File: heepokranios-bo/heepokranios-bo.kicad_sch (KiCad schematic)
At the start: 146 parts, among them J1 Conn_02x02_Odd_Even, J11 PGA_13x13, J14 Conn_02x03_Odd_Even, J15 Conn_02x08_Odd_Even, J16 Conn_02x03_Odd_Even, J17 Conn_02x03_Odd_Even, J2 Conn_02x02_Odd_Even, J21 Conn_01x02, J26 Conn_01x02, J27 Conn_01x02, J29 Conn_01x02, J3 Conn_02x03_Odd_Even, J30 Conn_01x02, J31 Conn_01x02, J32 Conn_01x02, J33 Conn_01x02, J34 Conn_01x02, J35 Conn_01x02, J36 Conn_01x02, J37 Conn_01x02, J38 Conn_01x02, J39 Conn_01x02, J4 Conn_02x03_Odd_Even, J40 Conn_01x02, J41 Conn_01x02, J42 Conn_01x02, J43 Conn_01x02, J48 Conn_01x02, J49 Conn_01x02, J5 Conn_02x03_Odd_Even, J6 Conn_02x04_Odd_Even, J8 Conn_02x03_Odd_Even, J9 Conn_02x02_Odd_Even, SW1 SW_Push, U1 BIWIN_DTS04GE_SMD

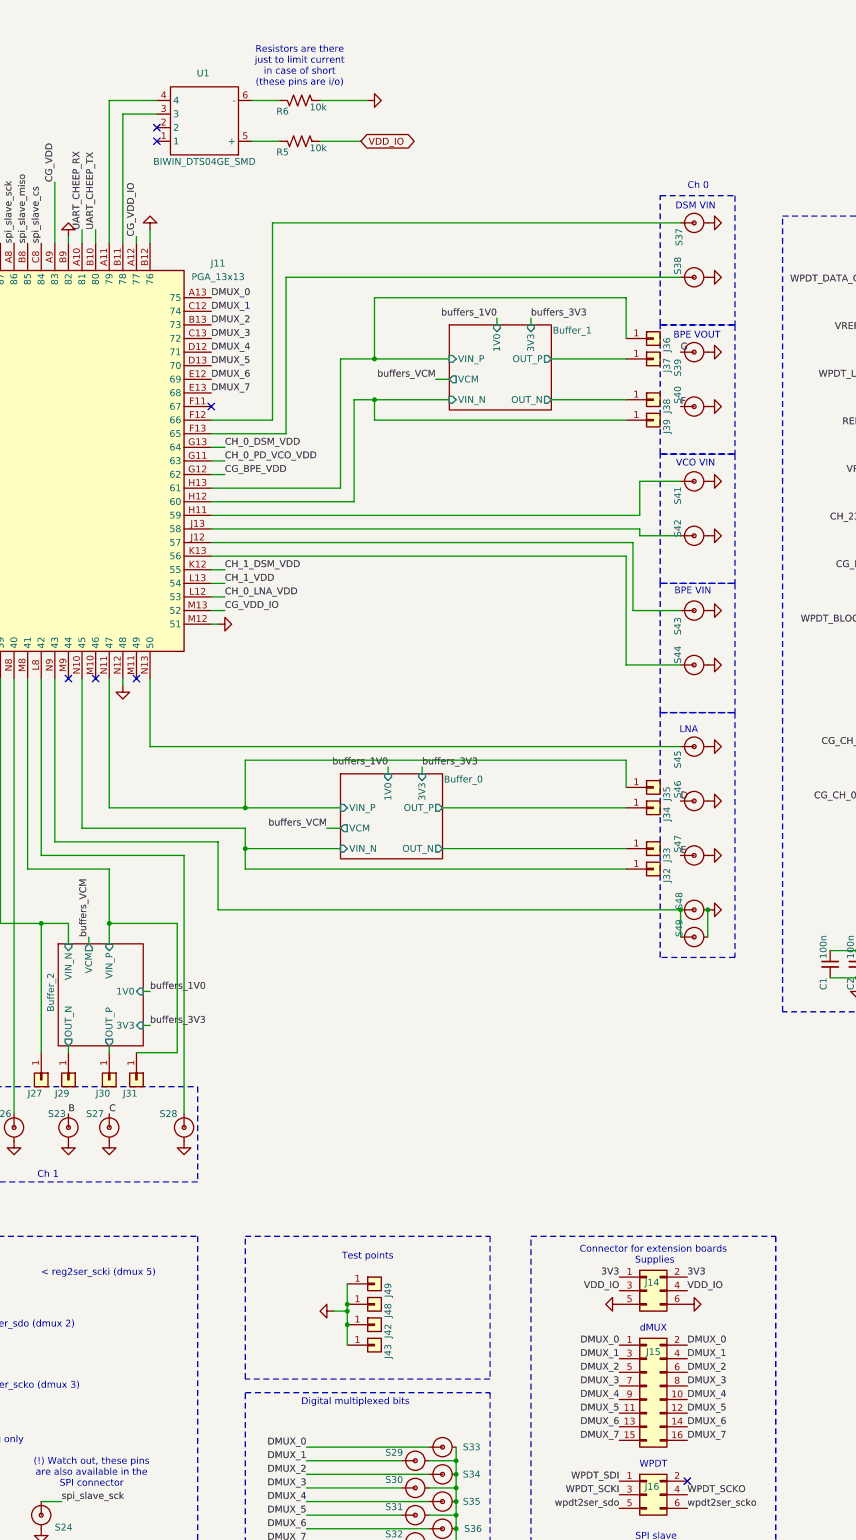
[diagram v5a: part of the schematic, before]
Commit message: Updated connector on bo
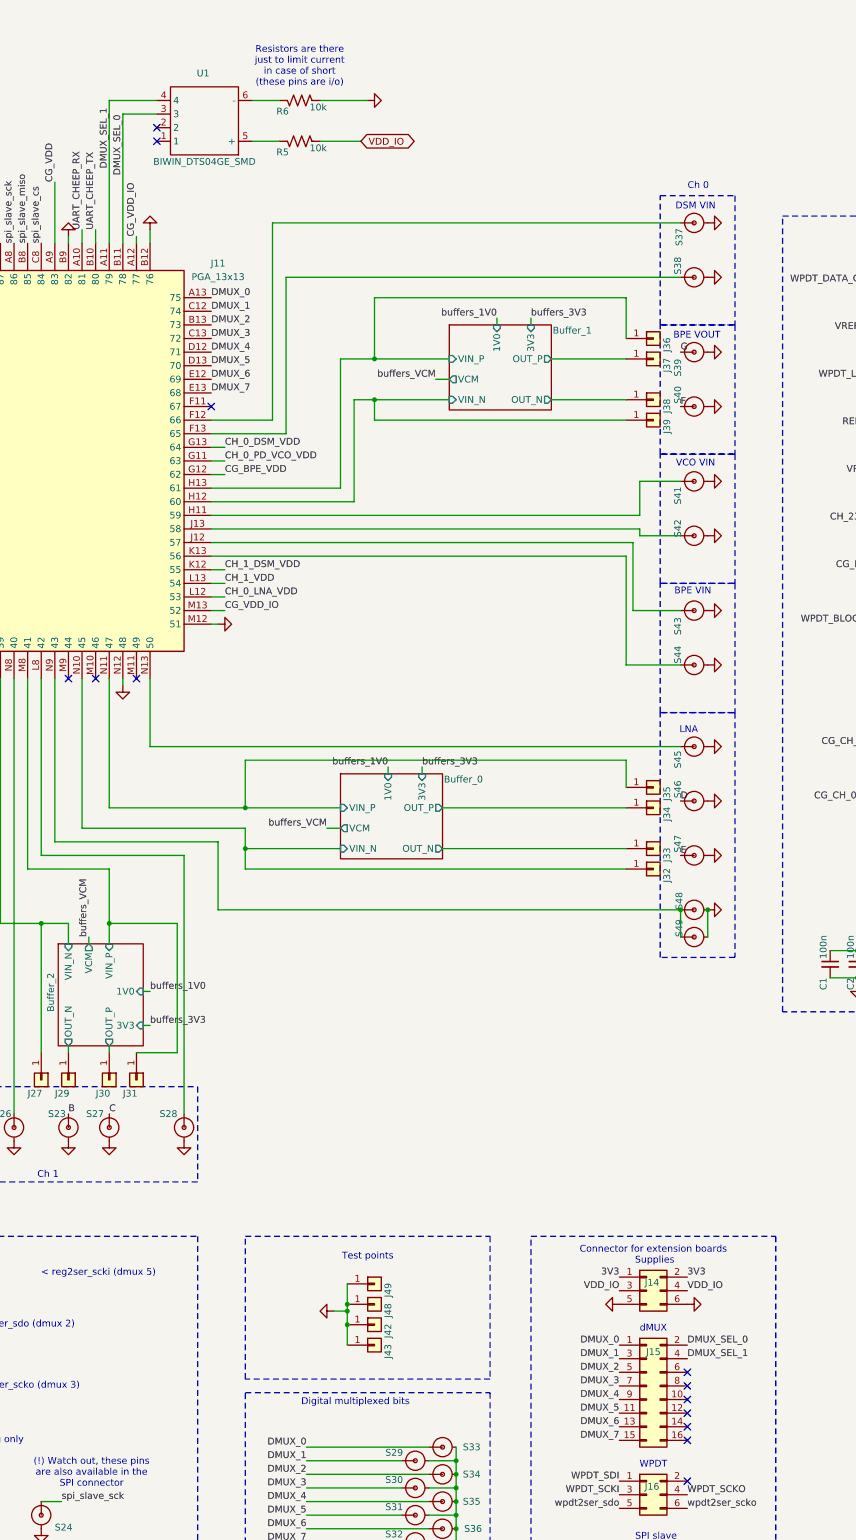
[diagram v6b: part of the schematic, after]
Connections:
- net DMUX_0: no longer J15.2 (Pin_2)
- net DMUX_1: no longer J15.4 (Pin_4)
- net DMUX_2: no longer J15.6 (Pin_6)
- net DMUX_3: no longer J15.8 (Pin_8)
- net DMUX_4: no longer J15.10 (Pin_10)
- net DMUX_5: no longer J15.12 (Pin_12)
- net DMUX_6: no longer J15.14 (Pin_14)
- net DMUX_7: no longer J15.16 (Pin_16)
- net DMUX_SEL_1: now reaches J11.A11 (79), U1.4
- net DMUX_SEL_1: now also J15.4 (Pin_4)
- net DMUX_SEL_0: now reaches J11.B11 (78), U1.3
- net DMUX_SEL_0: now also J15.2 (Pin_2)
- no-connect marks 112 -> 118
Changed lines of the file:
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@@
 	)
 	(no_connect
+		(at 394.97 364.49)
+	)
+	(no_connect
 		(at 209.55 86.36)
 	)
@@
 	)
 	(no_connect
+		(at 394.97 369.57)
+	)
+	(no_connect
 		(at 306.07 86.36)
 	)
@@
 	)
 	(no_connect
+		(at 394.97 367.03)
+	)
+	(no_connect
 		(at 224.79 86.36)
 	)
@@
 	)
 	(no_connect
+		(at 394.97 359.41)
+	)
+	(no_connect
 		(at 326.39 58.42)
 	)
@@
 	)
 	(no_connect
+		(at 394.97 361.95)
+	)
+	(no_connect
 		(at 295.91 127)
 	)
@@
 	)
 	(no_connect
+		(at 394.97 356.87)
+	)
+	(no_connect
 		(at 295.91 124.46)
 	)
@@
 		)
 	)
-	(label "DMUX_7"
-		(at 394.97 369.57 0)
-		(effects
-			(font
-				(size 1.27 1.27)
-			)
-			(justify left bottom)
-		)
-	)
 	(label "E"
 		(at 393.7 260.35 0)
@@
 		)
 	)
+	(label "DMUX_SEL_0"
+		(at 394.97 351.79 0)
+		(effects
+			(font
+				(size 1.27 1.27)
+			)
+			(justify left bottom)
+		)
+	)
 	(label "VDD_IO"
 		(at 226.06 121.92 0)
@@
 		)
 	)
-	(label "VREF_VIN"
-		(at 433.07 189.23 180)
+	(label "DMUX_SEL_1"
+		(at 394.97 354.33 0)
 		(effects
 			(font
 				(size 1.27 1.27)
 			)
-			(justify right bottom)
+			(justify left bottom)
 		)
 	)
-	(label "wpdt2ser_sdo"
-		(at 264.16 146.05 90)
+	(label "VREF_VIN"
+		(at 433.07 189.23 180)
 		(effects
 			(font
 				(size 1.27 1.27)
 			)
-			(justify left bottom)
+			(justify right bottom)
 		)
 	)
-	(label "DMUX_1"
-		(at 394.97 354.33 0)
+	(label "wpdt2ser_sdo"
+		(at 264.16 146.05 90)
 		(effects
 			(font
@@
 		)
 	)
-	(label "DMUX_2"
-		(at 394.97 356.87 0)
+	(label "DMUX_SEL_1"
+		(at 287.02 132.08 90)
 		(effects
 			(font
@@
 		)
 	)
-	(label "DMUX_6"
-		(at 394.97 367.03 0)
-		(effects
-			(font
-				(size 1.27 1.27)
-			)
-			(justify left bottom)
-		)
-	)
 	(label "nRST"
 		(at 186.69 114.3 180)
@@
 		)
 	)
+	(label "DMUX_SEL_0"
+		(at 289.56 133.35 90)
+		(effects
+			(font
+				(size 1.27 1.27)
+			)
+			(justify left bottom)
+		)
+	)
 	(label "DMUX_7"
 		(at 306.07 173.99 0)
@@
 		)
 	)
-	(label "DMUX_3"
-		(at 394.97 359.41 0)
-		(effects
-			(font
-				(size 1.27 1.27)
-			)
-			(justify left bottom)
-		)
-	)
 	(label "UART_CHEEP_RX"
 		(at 281.94 143.51 90)
@@
 		)
 	)
-	(label "DMUX_0"
-		(at 394.97 351.79 0)
-		(effects
-			(font
-				(size 1.27 1.27)
-			)
-			(justify left bottom)
-		)
-	)
 	(label "buffers_VCM"
 		(at 133.35 363.22 0)
@@
 		)
 	)
-	(label "DMUX_5"
-		(at 394.97 364.49 0)
-		(effects
-			(font
-				(size 1.27 1.27)
-			)
-			(justify left bottom)
-		)
-	)
 	(label "VREF_VIN"
 		(at 220.98 209.55 180)
@@
 		)
 	)
-	(label "DMUX_4"
-		(at 394.97 361.95 0)
-		(effects
-			(font
-				(size 1.27 1.27)
-			)
-			(justify left bottom)
-		)
-	)

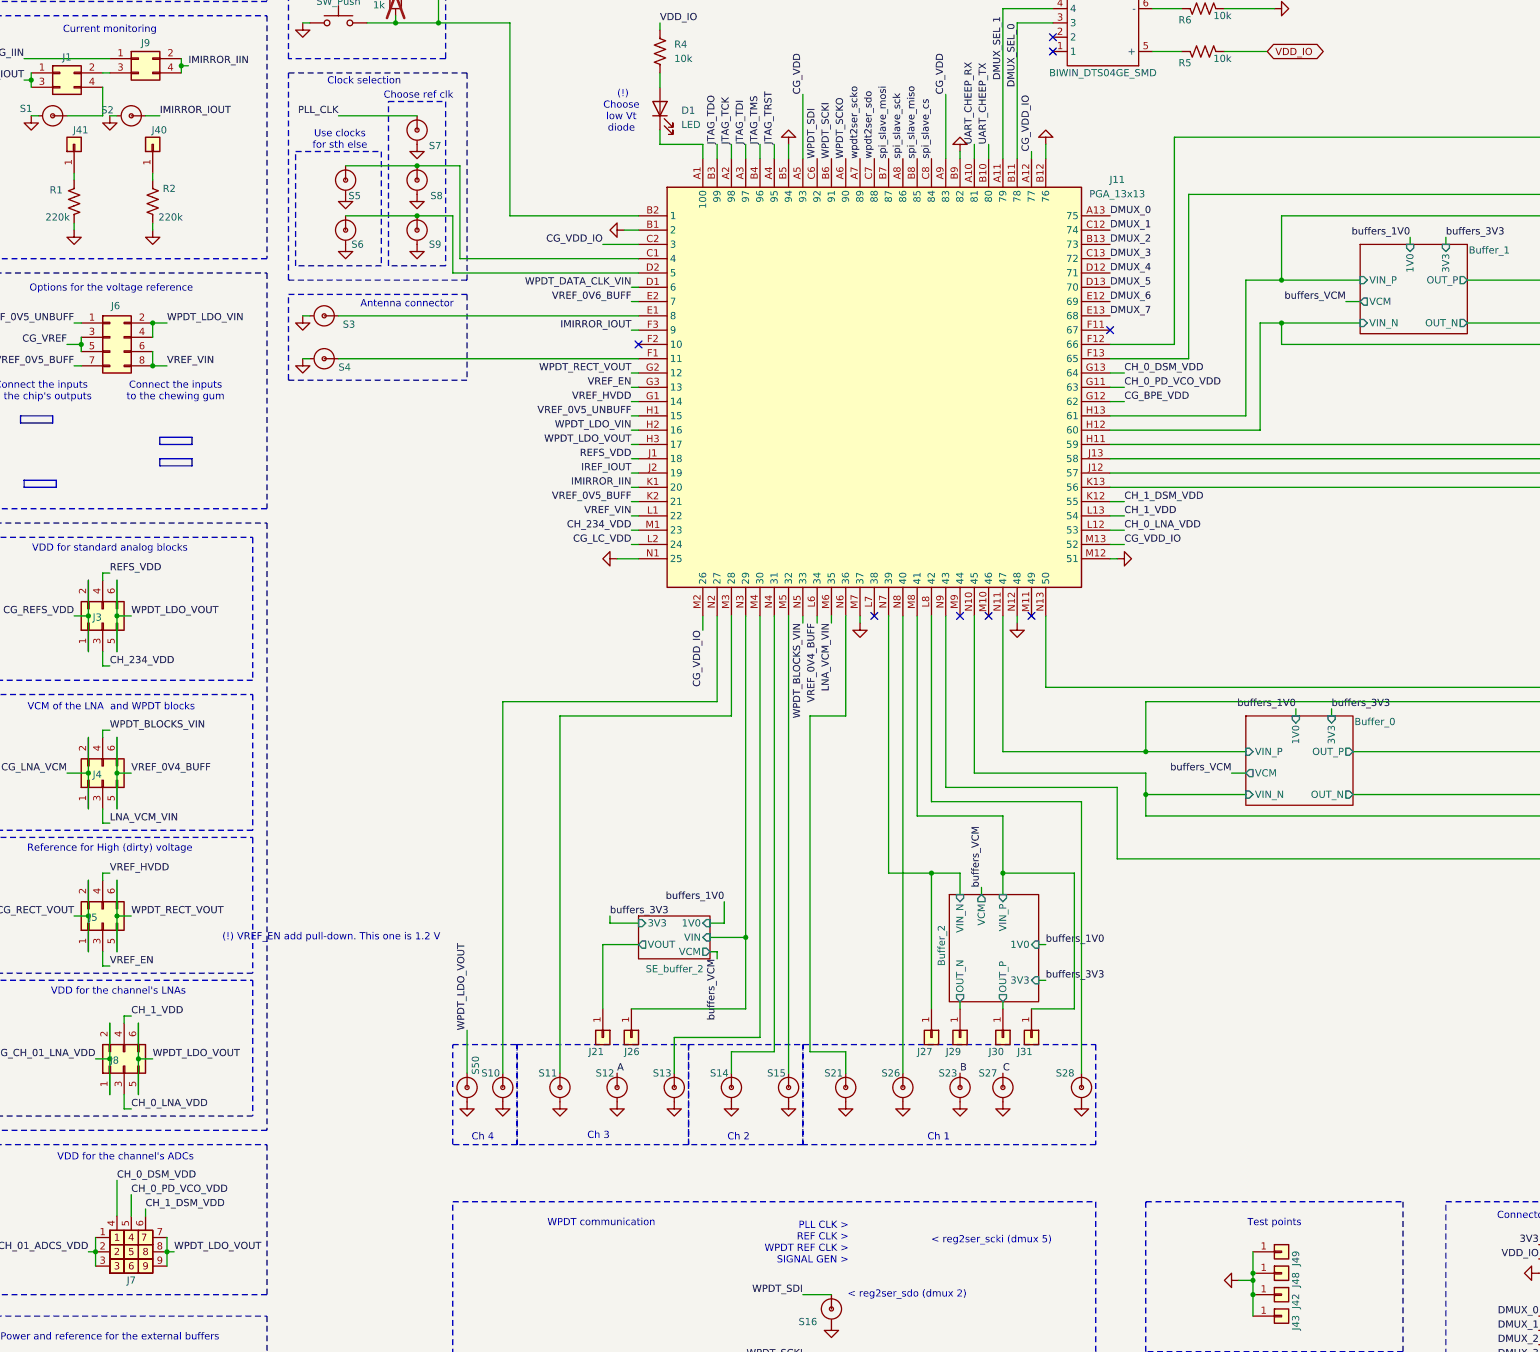
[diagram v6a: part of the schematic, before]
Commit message: Added matching circuit for antenna connector, and additional buffer for inputing SE and measuring FD
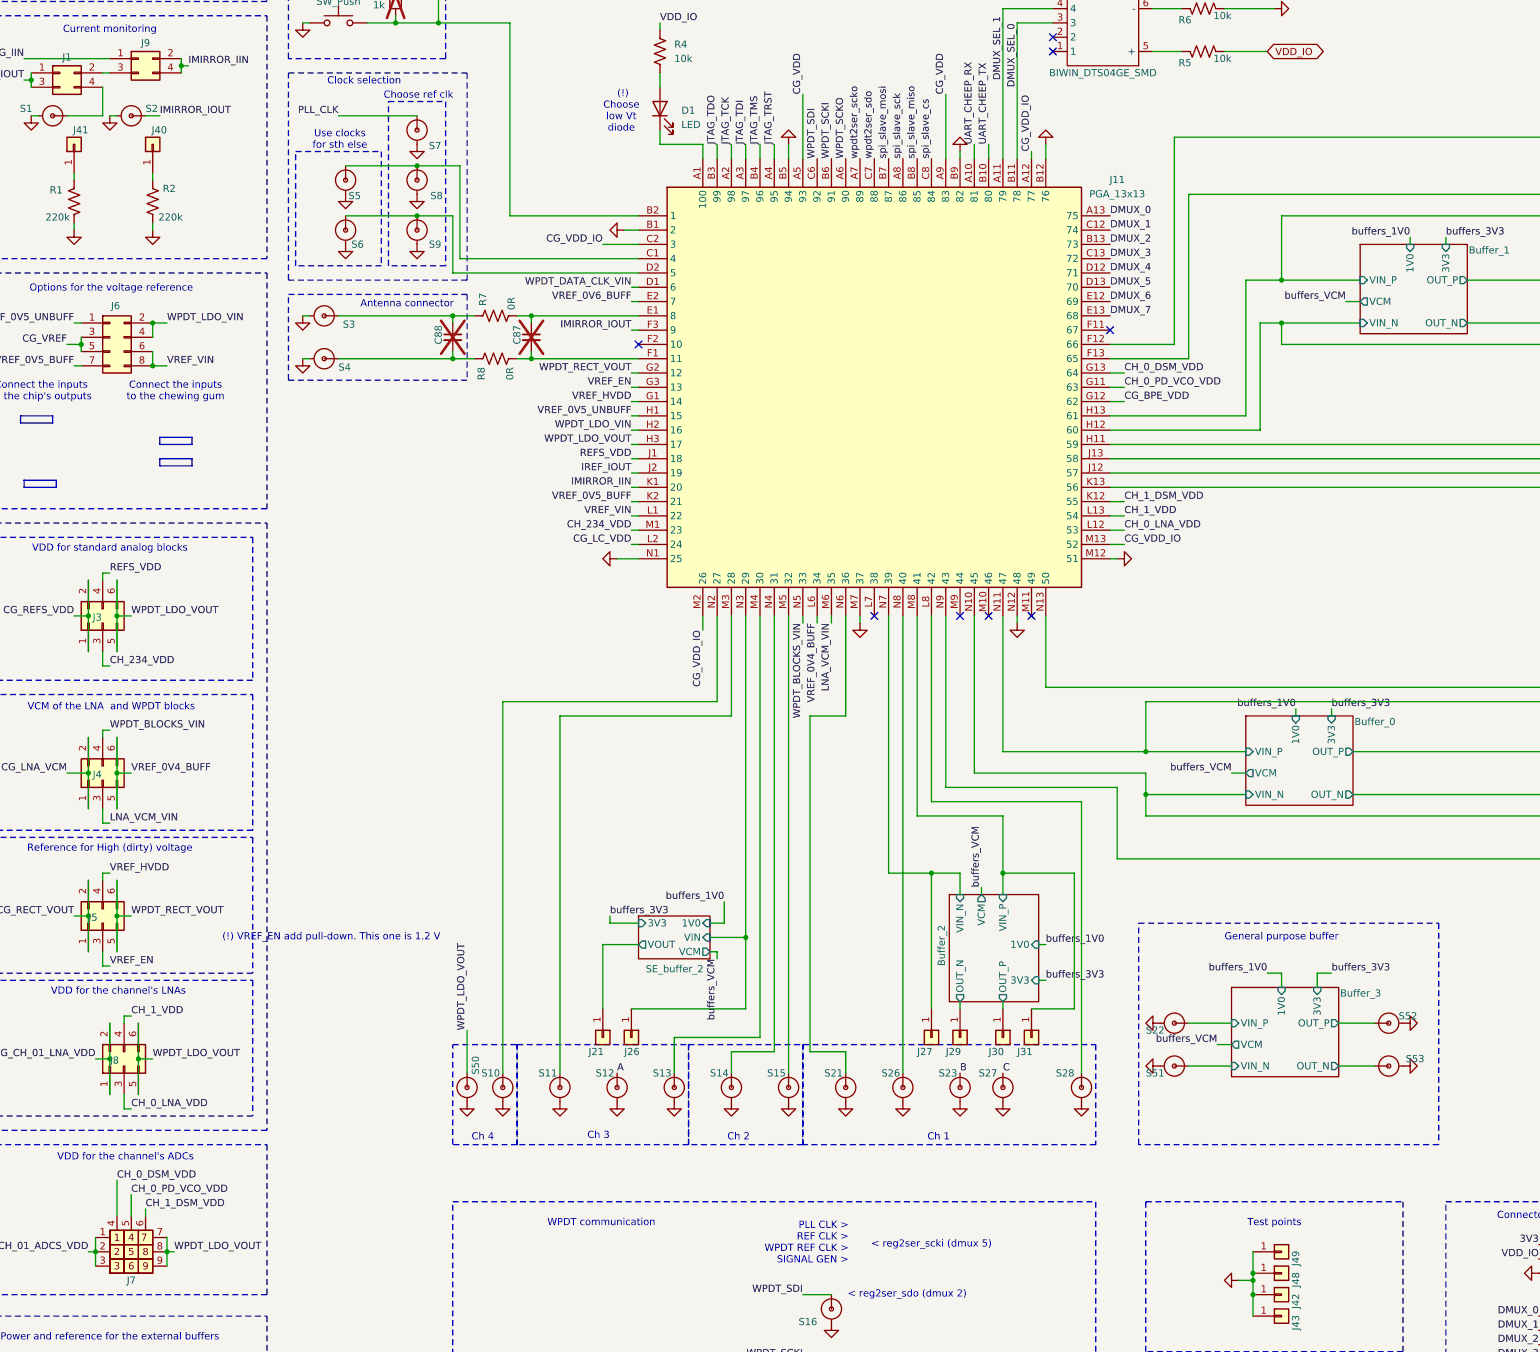
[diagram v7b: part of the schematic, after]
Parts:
- added C87, C88: (no value), Capacitor_SMD:C_0805_2012Metric_Pad1.18x1.45mm_HandSolder, symbol Device:C_Small
- added R7, R8: 0R, Resistor_SMD:R_0603_1608Metric, symbol Device:R_US
- added S22, S51, S52, S53: SMA connector, heepokranios-bo-library:SMA_w_tp, symbol heepokranios-bo-library:SMA_w_tp
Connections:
- net GND: now also S22.2, S51.2, S52.2, S53.2
- net at J11.E1 (8): now also C87.1, R7.2; no longer S3.1
- net at J11.F1 (11): now also C87.2, R8.2; no longer S4.1
- new net: C88.2, R8.1, S4.1
- new net: C88.1, R7.1, S3.1
- new net Buffer_3/OUT_N: S53.1
- new net Buffer_3/OUT_P: S52.1
- new net Buffer_3/VIN_N: S51.1
- new net Buffer_3/VIN_P: S22.1
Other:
- added sheet Buffer_3 (subsheets/fd_buffer.kicad_sch)
- note added: "General purpose buffer"

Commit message: Changed NC pins to gnd connections of substrate as per the bonding diagram
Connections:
- net GND: now also J11.F11 (67), J11.F2 (10), J11.L7 (38), J11.M10 (46), J11.M11 (49), J11.M9 (44)
- no-connect marks 118 -> 112
